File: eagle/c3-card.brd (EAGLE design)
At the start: 99.8 x 94.7 mm, 111 parts, among them J1 J-SAMTEC-TFM-110-X1-XXX-D-RA, J2 U.FL, J3 U.FL, J4 U.FL, J6 J-SAMTEC-TFM-120-X1-XXX-D-RA, J7 FTSH-105-XX-X-DV-K, Q3 MOSFET-PCH-SOT23-6, Q4 MOSFET-PCH-SOT23-6, Q5 PMV45EN, Q6 PMV45EN, U1 TCAN330, U2 IS21ES04G-JCLI-TR, U3 MAX7310ATE, U4 MAX4211CETE, U5 TPS62111RSA, U6 TCAN330, U7 MCP1703A, X1 16MHZ-2.5x2mm

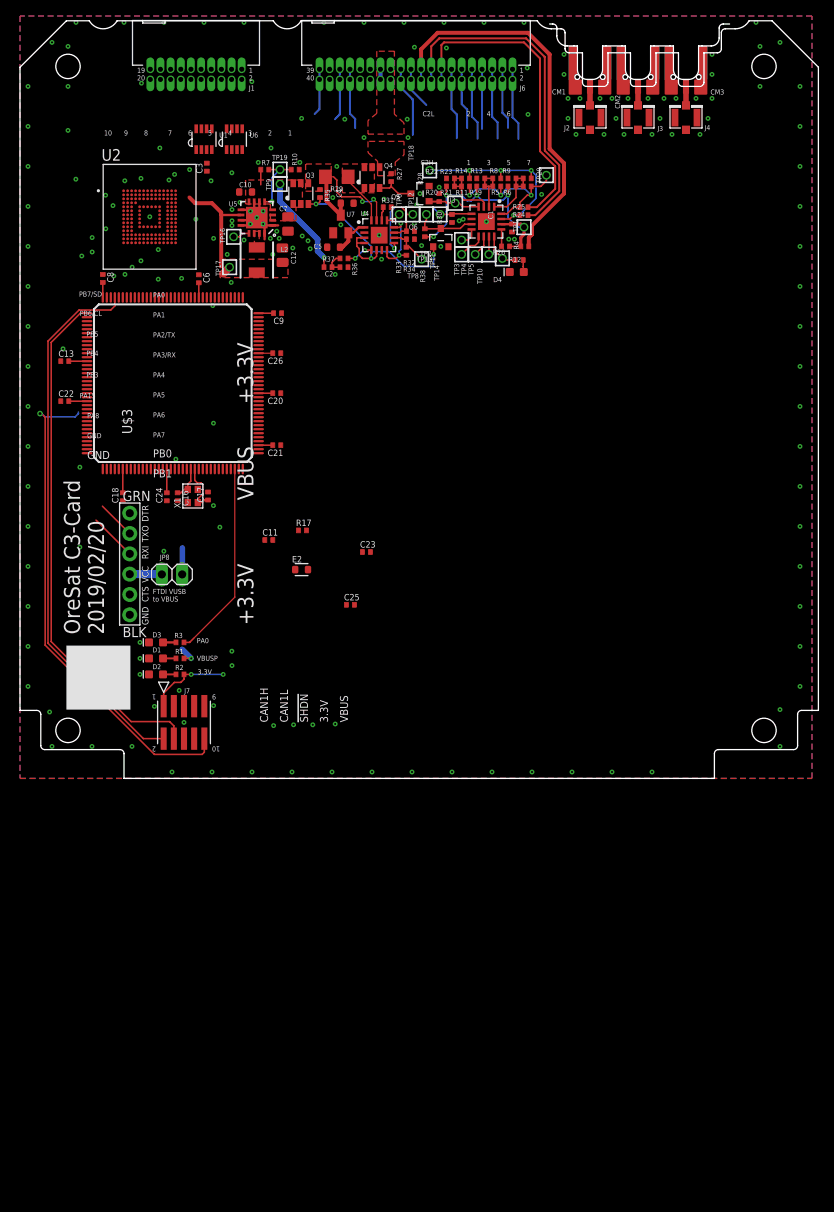
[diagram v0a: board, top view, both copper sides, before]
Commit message: Updated to the latest card outline. Updated OreSat main connector pinout. Got rid of some junk we don't need for C3.
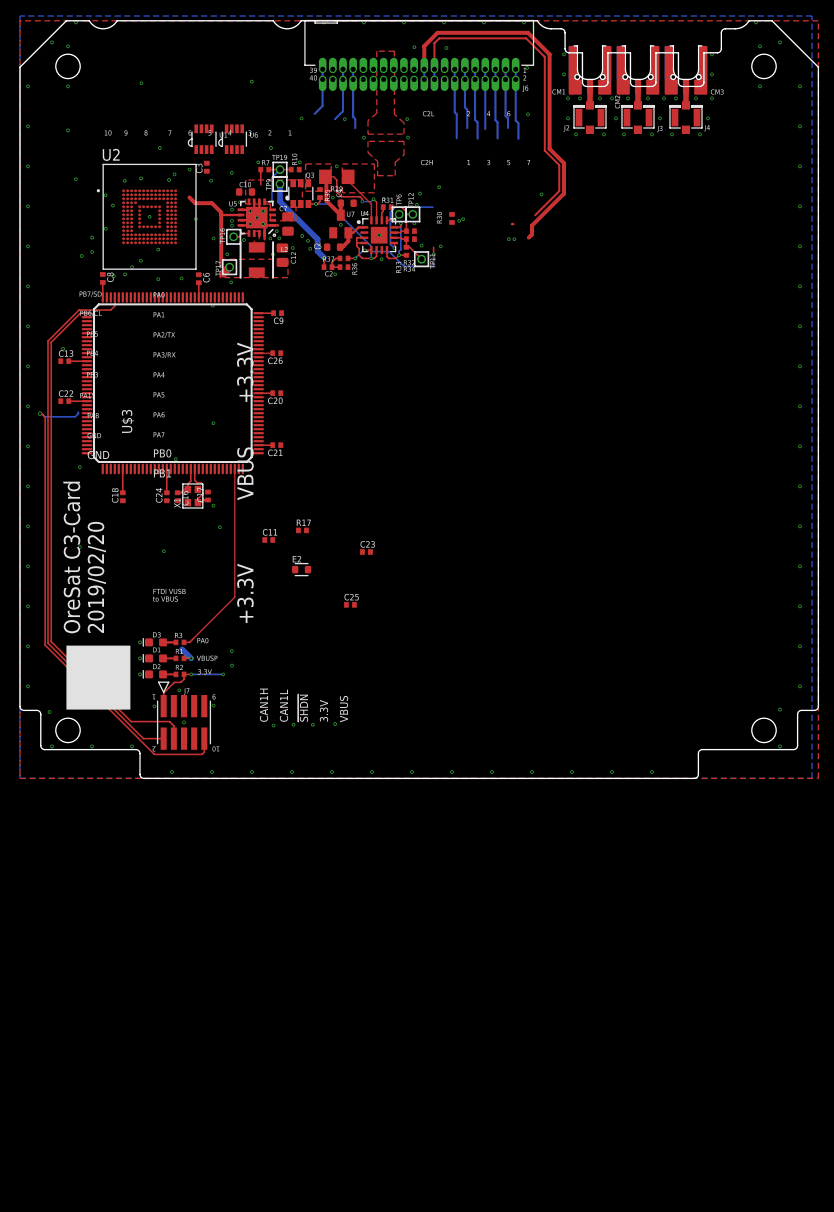
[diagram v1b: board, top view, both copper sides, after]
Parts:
- removed C1: 100n, rcl_custom:.0402-B-NOSILK
- removed D4: AMBER, SparkFun-LED:LED-0603
- removed J1: J-SAMTEC-TFM-110-X1-XXX-D-RA, J-Samtec-TFM-110-X1-XXX-D-RA:J-SAMTEC-TFM-110-X1-XXX-D-RA
- removed J5: (no value), SparkFun-Connectors:6_PIN_SERIAL_TARGET_SIDE_W_SILK
- removed JP8: (no value), pinhead:1X02
- removed Q4: MOSFET-PCH-SOT23-6, Q-MOSFET-PCH-SOT23-6:SOT23-6
- removed Q5, Q6: PMV45EN, Tova:SOT23
- removed R11, R13, R14, R19, R20, R21, R22, R23, R5, R6, R8, R9: NP, rcl_custom:.0402-B-NOSILK
- removed R12: 2.7k, rcl_custom:.0402-B-NOSILK
- removed R24, R25, R4: 100, rcl_custom:.0402-B-NOSILK
- removed R26, R27, R28, R38: 10k, rcl_custom:.0402-B-NOSILK
- removed TP1, TP10, TP13, TP14, TP18, TP2, TP20, TP3, TP4, TP5, TP8: TEST-POINT, Tova:2MM-TEST-POINT
- removed U3: MAX7310ATE, U-Maxim-MAX7310-I2C-GPIO-expander:QFN65P400X400X80-17T210
- U$2: value ORESAT-CARD-V1.1 -> ORESAT-CARD-V1.1-3XRF
- moved J6 0.40 mm to (49.9, 88.0)
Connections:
- net !SHUTDOWN renamed !SD
- removed net !FAULT: Q6.3, R38.1, TP8.1, U3.7
- removed net AD0: R5.1, R6.2, R8.2, R9.1, U3.1
- removed net AD1: R11.1, R13.2, R14.2, R19.1, U3.2
- removed net AD2: R20.1, R21.2, R22.2, R23.1, U3.3
- removed net AUX_!SHUTDOWN: J1.19, J1.20
- removed net AUX_CAN1_H: J1.13, J1.14
- removed net AUX_CAN1_L: J1.15, J1.16
- removed net AUX_CAN2_H: J1.1, J1.2
- removed net AUX_CAN2_L: J1.3, J1.4
- removed net AUX_GND1: J1.17, J1.18
- removed net AUX_GND2: J1.11, J1.12
- removed net AUX_GND3: J1.10, J1.9
- removed net AUX_VBUS1: J1.7, J1.8
- removed net AUX_VBUS2: J1.5, J1.6
- removed net CB-RESET: R30.2, TP14.1, U3.5, U4.9
- removed net N$406: J5.P$4, JP8.2
- removed net N$480: TP2.1, U3.8
- removed net N$482: TP3.1, U3.9
- removed net N$518: TP4.1, U3.10
- removed net N$523: TP5.1, U3.11
- removed net N$573: R12.2, TP10.1, U3.12
- removed net N$575: D4.A, R12.1
- removed net N$589: R26.1, U3.13
- removed net N$590: Q4.3, Q5.3, R27.1
- removed net N$593: Q4.1, Q4.2, Q4.5, Q4.6, R29.1, U4.16
- removed net ON/!OFF: Q5.1, R28.2, TP13.1, U3.4
- removed net PEN-SCL-FILT: R13.1, R21.1, R24.2, R6.1, TP18.1, U3.15
- removed net PEN-SDA-FILT: R19.2, R23.2, R25.2, R9.2, TP20.1, U3.16
- removed net SPARE6: J6.3, J6.4
- removed net SPARE7: J6.1, J6.2
- removed net VPD: C1.2, R11.2, R20.2, R26.2, R38.2, R4.2, R5.2, TP1.1, U3.14
- new net N$2: R30.2, U4.9
- net CAN2_H: now also J6.17, J6.18; no longer J6.21, J6.22
- net CAN2_L: now also J6.19, J6.20; no longer J6.23, J6.24
- net CB_CTRL: no longer Q6.1
- net GND: now also J6.27, J6.28; no longer C1.1, D4.C, J5.P$6, Q5.2, Q6.2, R14.1, R22.1, R28.1, R8.1, U3.6, U3.EPAD
- net OPD_PWR: now also J6.15, J6.16; no longer J6.19, J6.20, R4.1
- net OPD_SCL: now also J6.13, J6.14; no longer J6.17, J6.18, R24.1
- net OPD_SDA: now also J6.11, J6.12; no longer J6.15, J6.16, R25.1
- net PA2/USART2_TX: no longer J5.P$2
- net PA3/USART2_RX: no longer J5.P$3
- net SPARE1: now also J6.10, J6.9; no longer J6.13, J6.14
- net SPARE2: now also J6.7, J6.8; no longer J6.11, J6.12
- net SPARE3: now also J6.5, J6.6; no longer J6.10, J6.9
- net SPARE4: now also J6.3, J6.4; no longer J6.7, J6.8
- net SPARE5: now also J6.1, J6.2; no longer J6.5, J6.6
- net VBUS: now also J6.21, J6.22, J6.23, J6.24, R29.1, U4.16; no longer J6.27, J6.28, Q4.4, R27.2
- net VBUSP: no longer JP8.1
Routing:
- net OPD_PWR: track 48.4 -> 0.00 mm
- net CAN2_L: track 8.83 -> 47.1 mm
- net CAN2_H: track 5.27 -> 41.3 mm
- net OPD_SCL: track 42.4 -> 8.72 mm
- net OPD_SDA: track 39.0 -> 7.45 mm
- net VPD: track 31.5 -> 0.17 mm, vias 4 -> 0
- net PEN-SCL-FILT: track 25.7 -> 0.00 mm, vias 4 -> 0
- net PEN-SDA-FILT: track 20.3 -> 0.00 mm, vias 3 -> 0
- net CB-RESET: track 16.2 -> 0.00 mm, vias 1 -> 0
- net N$2: track 0.00 -> 11.1 mm, vias 0 -> 1
- net SPARE7: track 9.01 -> 0.00 mm
- net AD2: track 8.78 -> 0.00 mm
- net AD0: track 8.40 -> 0.00 mm
- net !FAULT: track 7.96 -> 0.00 mm
- net SPARE6: track 7.61 -> 0.00 mm
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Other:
- outline, holes or cut-outs redrawn

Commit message: Moved uC to new page
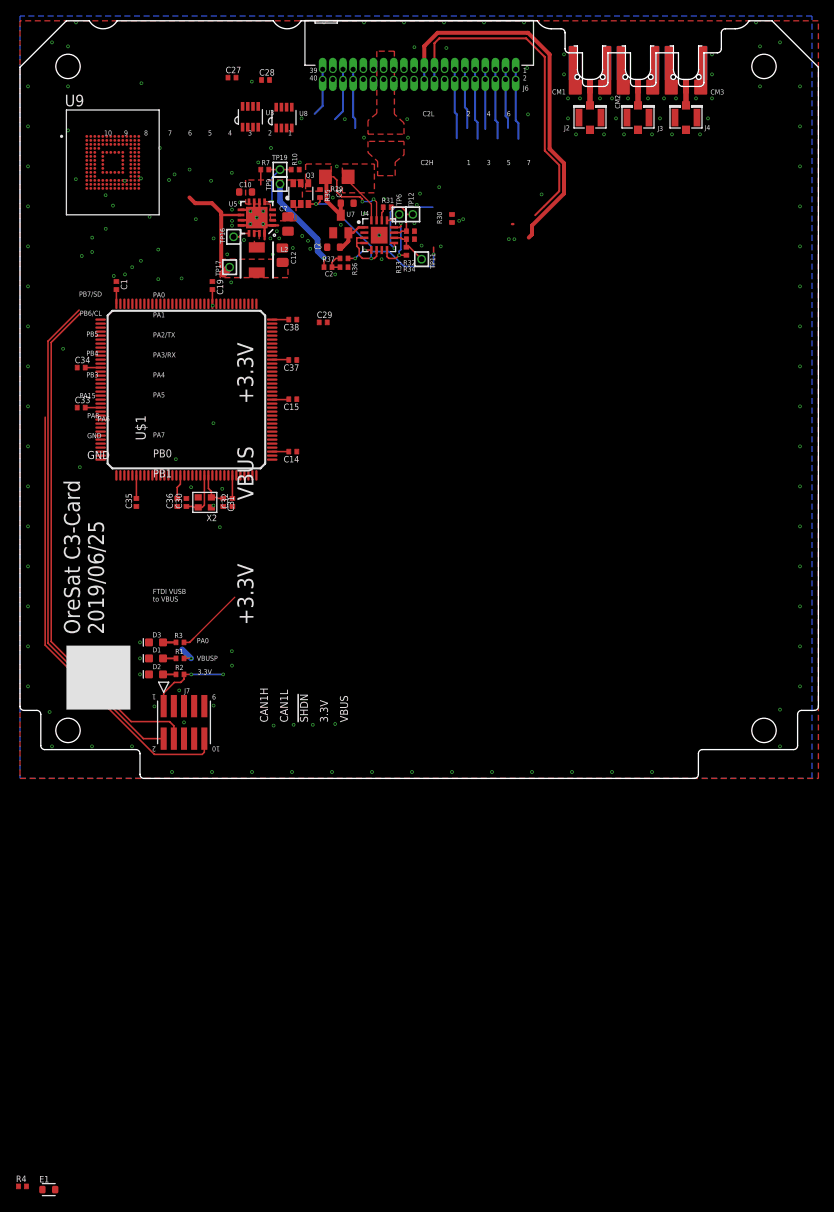
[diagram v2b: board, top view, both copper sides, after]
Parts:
- removed C11, C13, C18, C20, C21, C22, C23, C24, C25, C26, C3, C6, C8, C9: 100n, rcl_custom:.0402-B-NOSILK
- removed C16, C17: 20p, rcl_custom:.0402-B-NOSILK
- removed E2: (no value), oresat-rcl:.0603-B
- removed R17: 10k, rcl_custom:.0402-B-NOSILK
- removed U$3: STM32F446ZET6, U-ST-STM32F446RE-uC:P-TQFP-144-19
- removed U1, U6: TCAN330, TCAN330:SOT23-8_TI-DCN
- removed U2: IS21ES04G-JCLI-TR, IS21ES04G-JCLI-TR:BGA153N50P14X14_1150X1300X100
- removed X1: 16MHZ-2.5x2mm, low-gain-radio:CRYSTAL_2.5X2
- added C1, C14, C15, C19, C27, C28, C29, C32, C33, C34, C35, C36, C37, C38: 100n, rcl_custom:.0402-B-NOSILK
- added C30, C31: 20p, rcl_custom:.0402-B-NOSILK
- added E1: (no value), oresat-rcl:.0603-B
- added R4: 10k, rcl_custom:.0402-B-NOSILK
- added U$1: STM32F446ZET6, U-ST-STM32F446RE-uC:P-TQFP-144-19
- added U3, U8: TCAN330, TCAN330:SOT23-8_TI-DCN
- added U9: IS21ES04G-JCLI-TR, IS21ES04G-JCLI-TR:BGA153N50P14X14_1150X1300X100
- added X2: 16MHZ-2.5x2mm, low-gain-radio:CRYSTAL_2.5X2
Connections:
- removed net CRYSTALIN2: C17.1, U$3.24, X1.1
- removed net CRYSTALOUT2: C16.1, U$3.23, X1.3
- removed net N$6: R17.2, U$3.138
- removed net N$7: E2.2, U$3.33
- new net CRYSTALIN1: C31.1, U$1.24, X2.1
- new net CRYSTALOUT1: C30.1, U$1.23, X2.3
- new net N$3: R4.2, U$1.138
- new net N$4: E1.2, U$1.33
- net 3.3V: now also C1.2, C14.2, C15.2, C19.2, C27.2, C28.2, C29.2, C32.2, C33.2, C34.2, C35.2, C36.2, C37.2, C38.2, E1.1, U$1.108, U$1.121, U$1.131, U$1.144, U$1.17, U$1.30, U$1.39, U$1.52, U$1.6, U$1.62, U$1.72, U$1.84, U3.3, U8.3, U9.C6, U9.E6, U9.F5, U9.J10, U9.K9, U9.M4, U9.N4, U9.P3, U9.P5; no longer C11.2, C13.2, C18.2, C20.2, C21.2, C22.2, C23.2, C24.2, C25.2, C26.2, C3.2, C6.2, C8.2, C9.2, E2.1, U$3.108, U$3.121, U$3.131, U$3.144, U$3.17, U$3.30, U$3.39, U$3.52, U$3.6, U$3.62, U$3.72, U$3.84, U1.3, U2.C6, U2.E6, U2.F5, U2.J10, U2.K9, U2.M4, U2.N4, U2.P3, U2.P5, U6.3
- net CAN1_H: now also U3.7; no longer U1.7
- net CAN1_L: now also U3.6; no longer U1.6
- net CAN1_RX: now also U$1.103, U3.4; no longer U$3.103, U1.4
- net CAN1_SHDN: now also U$1.102, U3.5; no longer U$3.102, U1.5
- net CAN1_SILENT: now also U$1.101, U3.8; no longer U$3.101, U1.8
- net CAN1_TX: now also U$1.104, U3.1; no longer U$3.104, U1.1
- net CAN2_H: now also U8.7; no longer U6.7
- net CAN2_L: now also U8.6; no longer U6.6
- net CAN2_RX: now also U$1.73, U8.4; no longer U$3.73, U6.4
- net CAN2_SHDN: now also U$1.70, U8.5; no longer U$3.70, U6.5
- net CAN2_SILENT: now also U$1.69, U8.8; no longer U$3.69, U6.8
- net CAN2_TX: now also U$1.74, U8.1; no longer U$3.74, U6.1
- net GND: now also C1.1, C14.1, C15.1, C19.1, C27.1, C28.1, C29.1, C30.2, C31.2, C32.1, C33.1, C34.1, C35.1, C36.1, C37.1, C38.1, R4.1, U$1.107, U$1.120, U$1.130, U$1.16, U$1.31, U$1.38, U$1.51, U$1.61, U$1.83, U$1.94, U3.2, U8.2, U9.A6, U9.C4, U9.E7, U9.G5, U9.H10, U9.J5, U9.K8, U9.N2, U9.N5, U9.P4, U9.P6, X2.2, X2.4; no longer C11.1, C13.1, C16.2, C17.2, C18.1, C20.1, C21.1, C22.1, C23.1, C24.1, C25.1, C26.1, C3.1, C6.1, C8.1, C9.1, R17.1, U$3.107, U$3.120, U$3.130, U$3.16, U$3.31, U$3.38, U$3.51, U$3.61, U$3.83, U$3.94, U1.2, U2.A6, U2.C4, U2.E7, U2.G5, U2.H10, U2.J5, U2.K8, U2.N2, U2.N5, U2.P4, U2.P6, U6.2, X1.2, X1.4
- net NRESET: now also U$1.25; no longer U$3.25
- net PA0: now also U$1.34; no longer U$3.34
- net PA2/USART2_TX: now also U$1.36; no longer U$3.36
- net PA3/USART2_RX: now also U$1.37; no longer U$3.37
- net SWCLK: now also U$1.109; no longer U$3.109
- net SWDIO: now also U$1.105; no longer U$3.105
- net VDDI: now also U9.C2; no longer U2.C2
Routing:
- net PA0: track 24.7 -> 8.69 mm
- net NRESET: track 62.0 -> 55.9 mm, vias 1 -> 0
- net CRYSTALOUT1: track 0.00 -> 6.14 mm
- net CRYSTALIN2: track 6.04 -> 0.00 mm
- net SWDIO: track 68.4 -> 62.7 mm
- net CRYSTALIN1: track 0.00 -> 4.43 mm
- net CRYSTALOUT2: track 4.19 -> 0.00 mm
- net 3.3V: track 46.9 -> 49.8 mm
- net SWCLK: track 64.7 -> 63.9 mm
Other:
- board text added: "2019/06/25"
- board text removed: "2019/02/20"
